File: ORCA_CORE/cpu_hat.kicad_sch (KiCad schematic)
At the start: 14 parts, among them J17 data_line_power, J31 I2C_1, J32 I2C_2, J49 USB_B_Micro, J53 cover_left, J54 base_left, J59 base_right, J60 cover_right

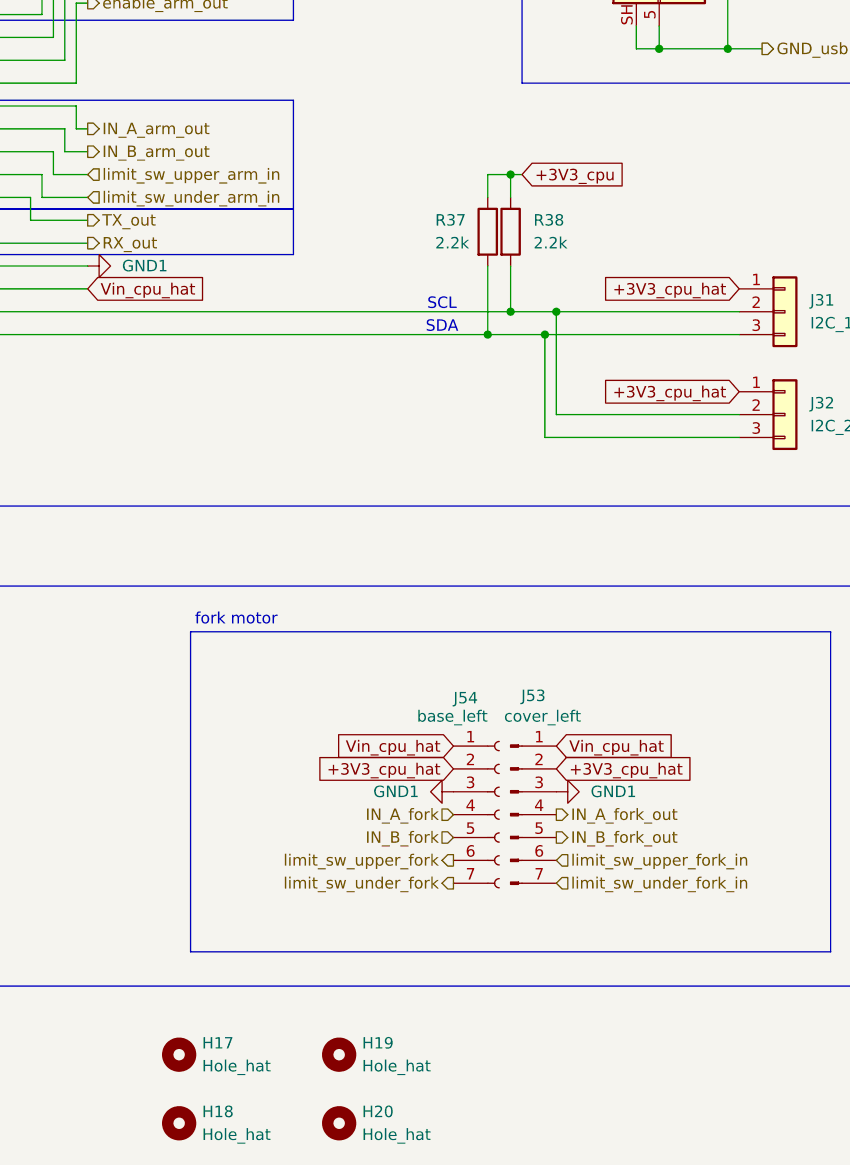
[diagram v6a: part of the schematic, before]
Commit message: complete almost all wires. add mouse coms sensor
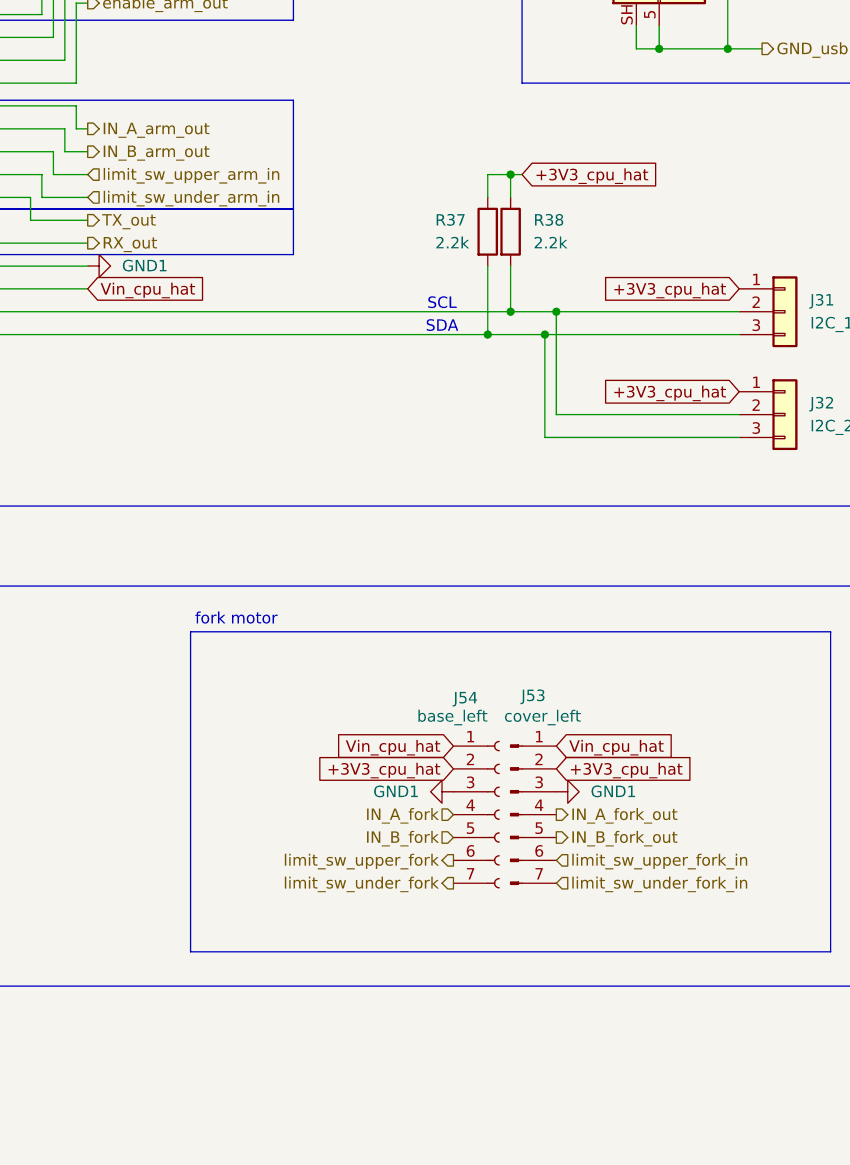
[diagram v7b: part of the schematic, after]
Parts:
- removed H17, H18, H19, H20: Hole_hat, MountingHole:MountingHole_3.2mm_M3, symbol Mechanical:MountingHole
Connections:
- net +3V3_cpu is gone; now on net +3V3_cpu_hat: R37.1, R38.1

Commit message: end wiring
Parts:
- added U14: BNO055, IMU:BNO055, symbol mylib:BNO055
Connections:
- net +3V3_cpu_hat: now also U14.1 (VDD)
- net GND1: now also U14.2 (GND), U14.7 (GND)
- net at J31.2 (Pin_2), J32.2 (Pin_2), J60.14 (Pin_14)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: now also U14.4 (SCL)
- net at J31.3 (Pin_3), J32.3 (Pin_3), J60.12 (Pin_12)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: now also U14.3 (SDA)
- no-connect marks 0 -> 3
